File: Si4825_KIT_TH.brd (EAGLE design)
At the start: 57.1 x 38.1 mm, 26 parts, among them U1 SI4825, U2 LMV358SOIC, Y1 32.768kHz

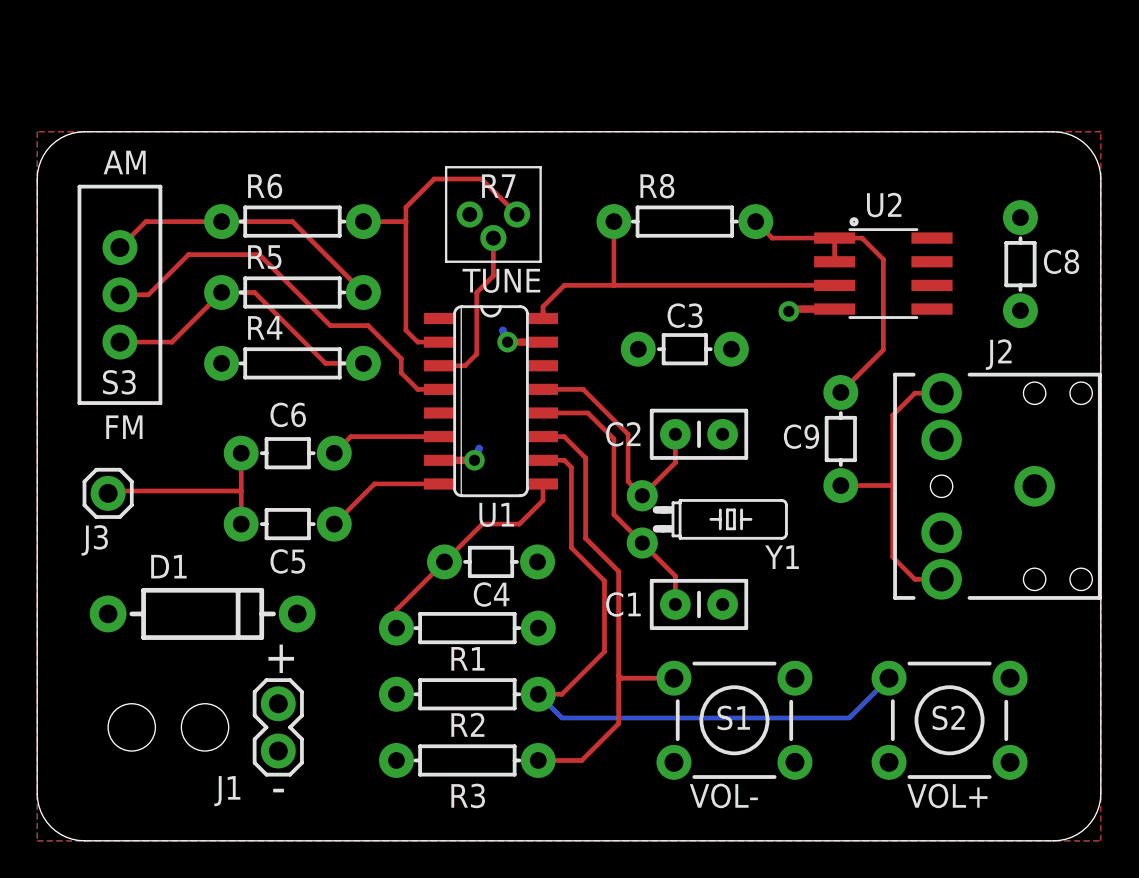
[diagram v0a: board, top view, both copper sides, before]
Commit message: Fixed issues discovered in first build
- fixed potentiometer footprint
- bigger strain relief holes: .1” to .15”
- changed U2 (op amp) to through hole version
- changed value of C9 (AC coupling capacitor) to 22uF in BOM and
schematic
- Removed R8 (jumper to bypass op amp)
- Regenerated gerbers, jpg previews, and pdf of schematic
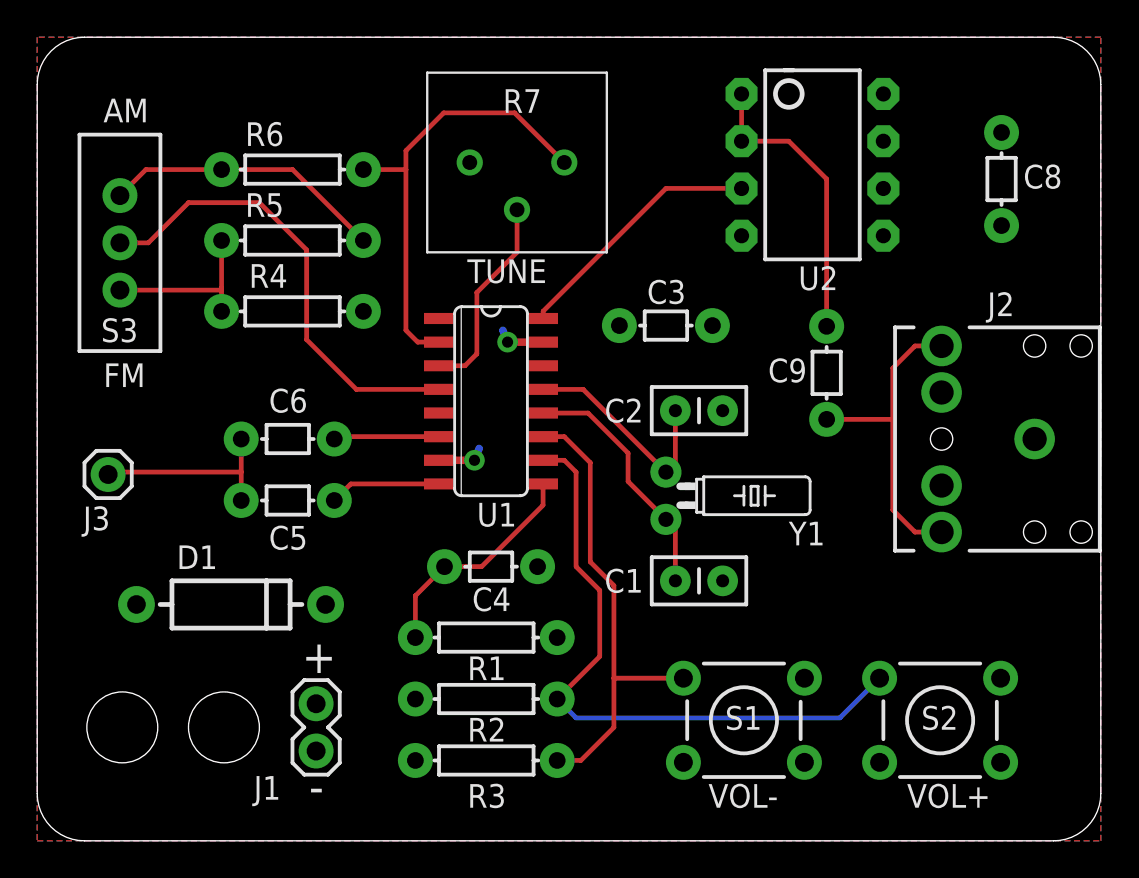
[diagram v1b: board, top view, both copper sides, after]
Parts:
- removed R8: 0, SparkFun-Resistors:AXIAL-0.3
- C9: value 1uF -> 22uF
- U2: value LMV358SOIC -> LM358; device SparkFun-AnalogIC:SO08 -> SparkFun-AnalogIC:DIP08
- moved U2 6.97 mm to (41.7, 36.3)
- moved C8 4.68 mm to (51.8, 35.6)
- moved C9 3.64 mm to (42.4, 25.1)
- moved R7 3.07 mm to (25.8, 36.4)
- moved R5 2.79 mm to (13.7, 32.3)
- moved R4 2.79 mm to (13.7, 28.4), turned to 180 degrees
- moved S3 2.79 mm to (4.45, 32.1)
- moved R6 2.79 mm to (13.7, 36.1)
- moved J2 2.54 mm to (53.6, 21.6)
- moved J1 2.03 mm to (15.0, 4.83)
- moved Y1 1.80 mm to (33.8, 18.5)
- moved C3 1.63 mm to (33.8, 27.7)
- moved D1 1.61 mm to (10.4, 12.7)
- moved C1 1.27 mm to (34.3, 14.0)
- moved C2 1.27 mm to (34.3, 23.1)
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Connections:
- net N$13: no longer R8.P$2
- net N$14: no longer R8.P$1
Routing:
- net N$14: track 20.6 -> 13.8 mm
- net N$8: track 15.8 -> 9.27 mm
- net N$10: track 18.3 -> 24.4 mm
- net N$7: track 21.5 -> 25.0 mm
- net N$5: track 37.1 -> 34.3 mm
- net GND: track 7.71 -> 5.19 mm, vias 3 -> 2
- net N$12: track 8.89 -> 10.9 mm
- net N$3: track 13.2 -> 12.0 mm
- net N$2: track 14.6 -> 13.4 mm
- net N$13: track 17.1 -> 15.9 mm
- net N$18: track 16.7 -> 17.4 mm
- net N$1: track 6.52 -> 5.99 mm
- net N$15: track 11.0 -> 10.5 mm
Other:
- board size 57.1 x 38.1 mm -> 57.1 x 43.2 mm
